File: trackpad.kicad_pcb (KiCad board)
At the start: 2 copper layers, 172 x 125.9 mm, 68 parts, among them J1 type-c-31-m-12, J10 Conn_01x01_Pin, J3 JST 3P, J5 Conn_01x07_Pin, J9 Conn_01x02_Pin, SW1 SW_Push, SW2 SW_Push, SW3 SW_Push, SW4 SW_Push, U1 RP2040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

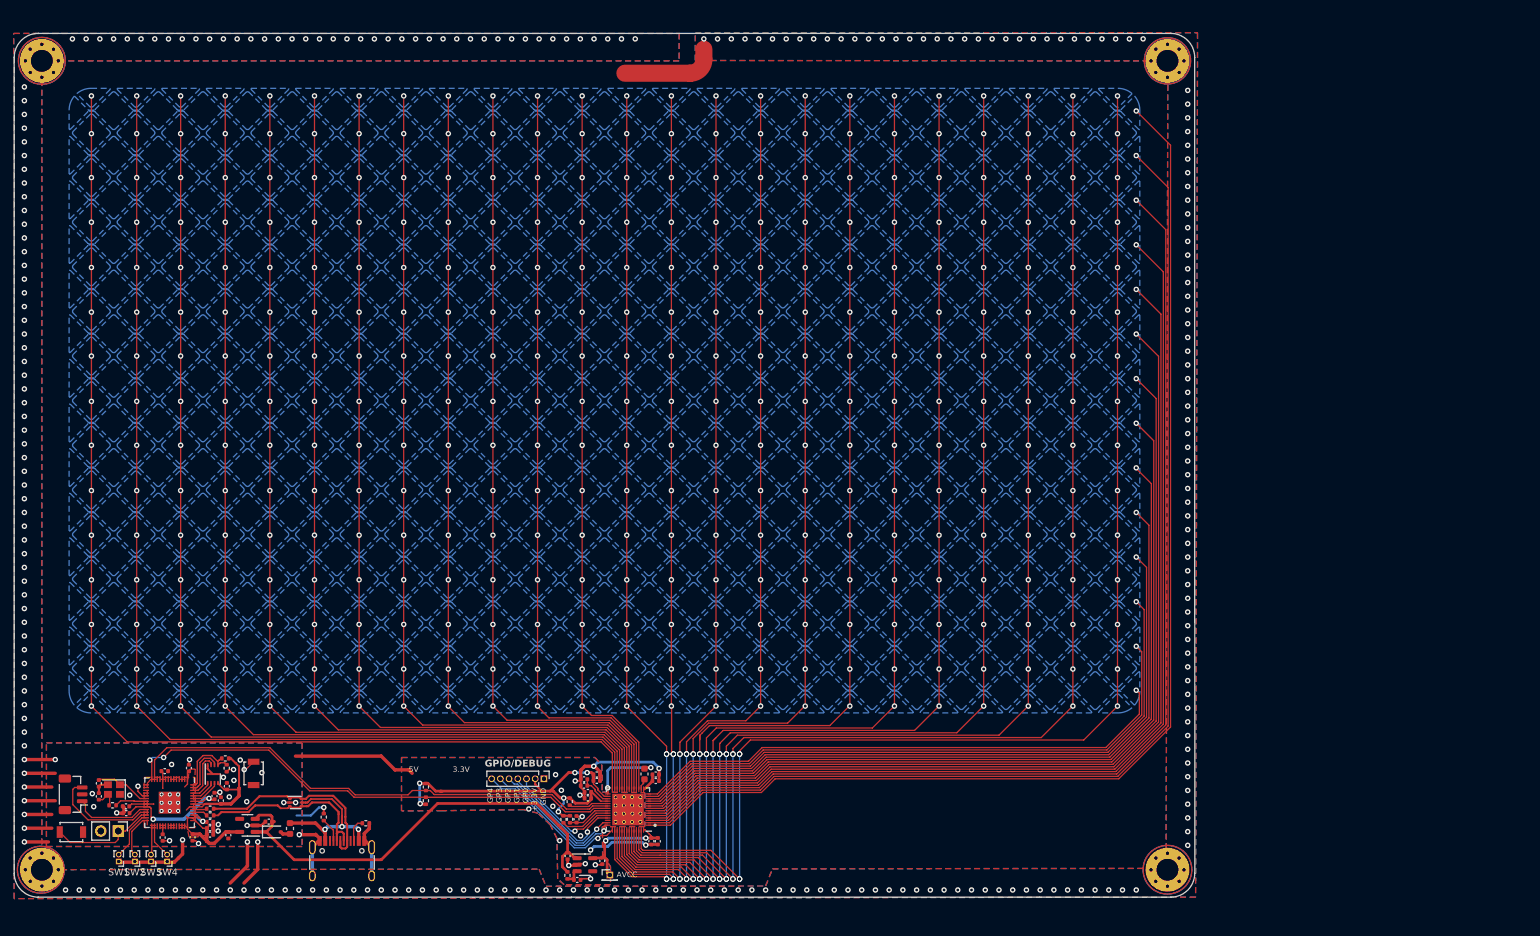
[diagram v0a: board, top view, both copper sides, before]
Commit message: made some adjustments to the gnd planes and connections
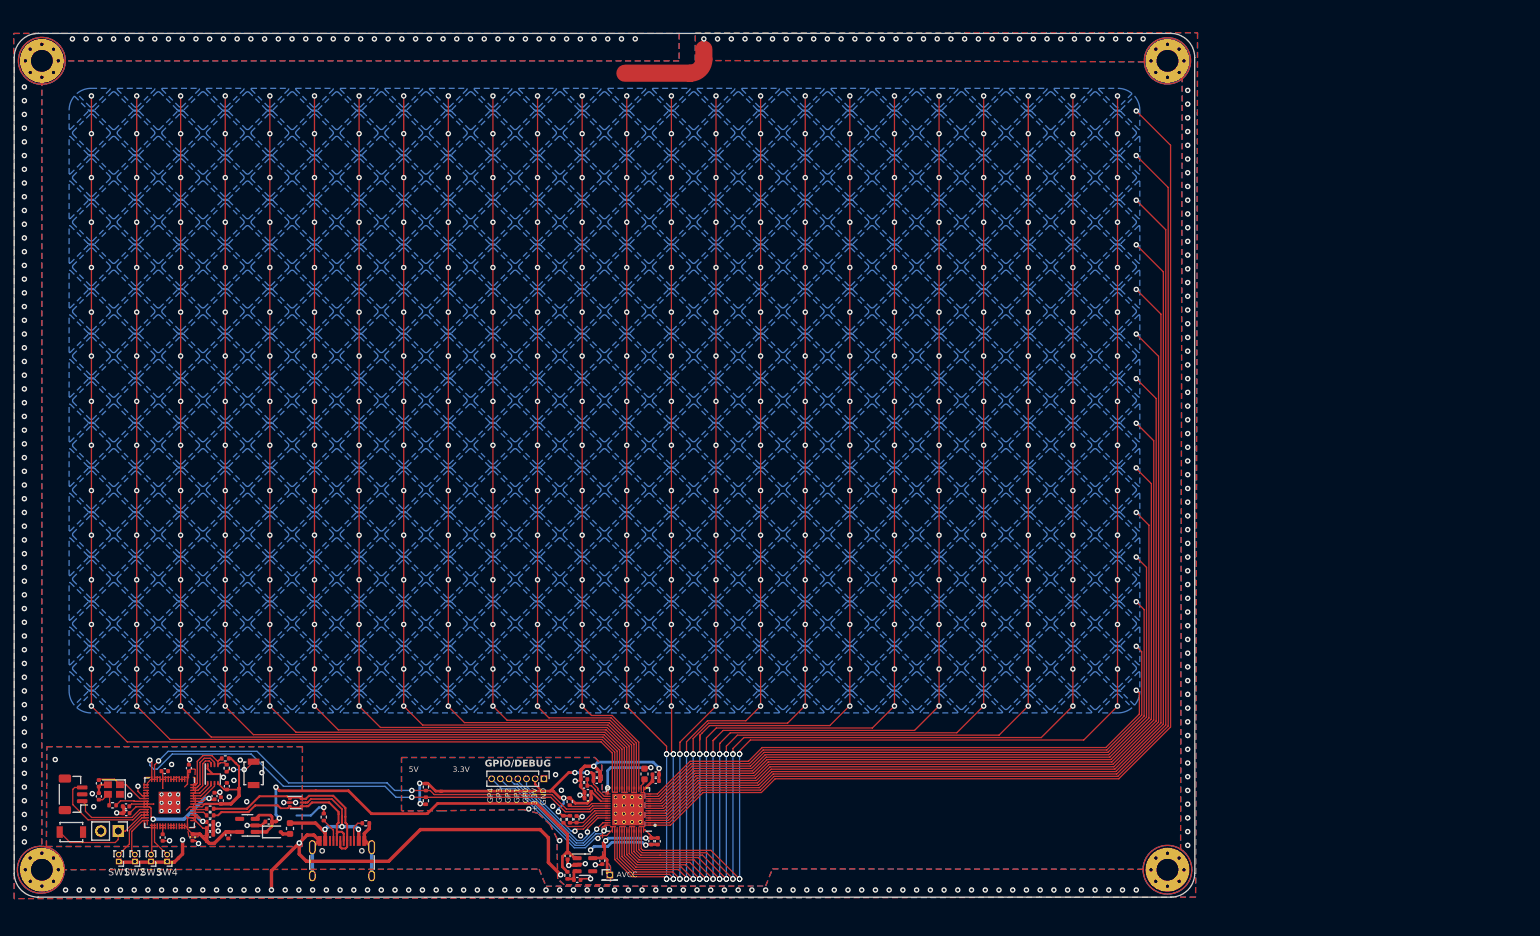
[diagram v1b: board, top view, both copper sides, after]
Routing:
- net (no net): track 31.9 -> 0.00 mm, vias 4 -> 2
- net GND: track 141.5 -> 168.2 mm, vias 317 -> 318
- net Net-(R2-Pad1): track 2.98 -> 4.53 mm
- net 5V: track 66.1 -> 67.6 mm, vias 0 -> 2
- net SDA: track 73.9 -> 72.5 mm, vias 0 -> 2
- net SCL: track 74.0 -> 75.1 mm

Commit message: rotated things in the PCB editor so its orientation matches intended use.
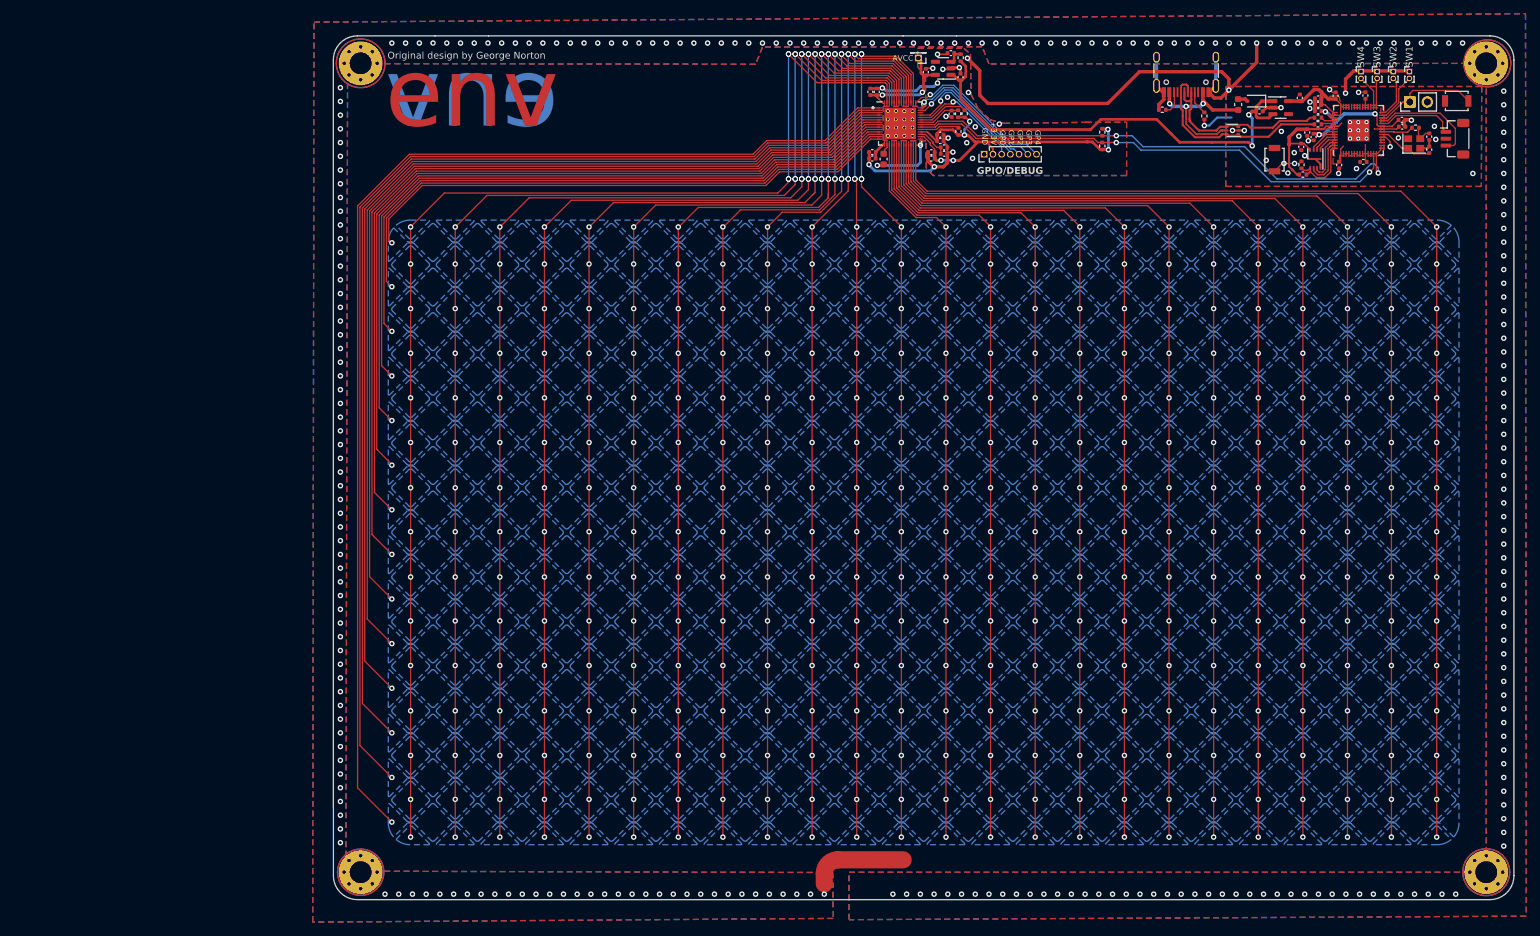
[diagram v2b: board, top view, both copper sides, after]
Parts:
- moved H3 241.4 mm to (239.0, 153.4), turned to 180 degrees
- moved H4 241.0 mm to (239.0, 35.6), turned to 180 degrees
- moved SW_RST1 228.2 mm to (234.7, 41.0), turned to 180 degrees
- moved J3 222.9 mm to (234.4, 46.5), turned to -90 degrees
- moved SW1 220.5 mm to (227.8, 36.8), turned to 0 degrees
- moved SW2 216.5 mm to (225.4, 36.8), turned to 0 degrees
- moved C13 216.4 mm to (230.7, 46.2), turned to -90 degrees
- moved J9 216.1 mm to (227.9, 41.2), turned to 90 degrees
- moved C12 214.7 mm to (230.7, 48.1), turned to 90 degrees
- moved R3 214.0 mm to (228.7, 44.9), turned to 0 degrees
- moved SW3 212.5 mm to (223.1, 36.8), turned to 0 degrees
- moved Y1 211.5 mm to (228.5, 47.2), turned to 0 degrees
- moved C3 211.5 mm to (226.7, 43.8), turned to 0 degrees
- moved C8 210.7 mm to (226.7, 44.8), turned to 0 degrees
- moved SW4 208.6 mm to (220.7, 36.8), turned to 0 degrees
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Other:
- board size 172 x 125.9 mm -> 172 x 125.8 mm
- board text added: "Original design by George Norton"
- board text added: "env"
- board text removed: "3.3V"
- board text removed: "5V"

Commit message: added some art, might remove
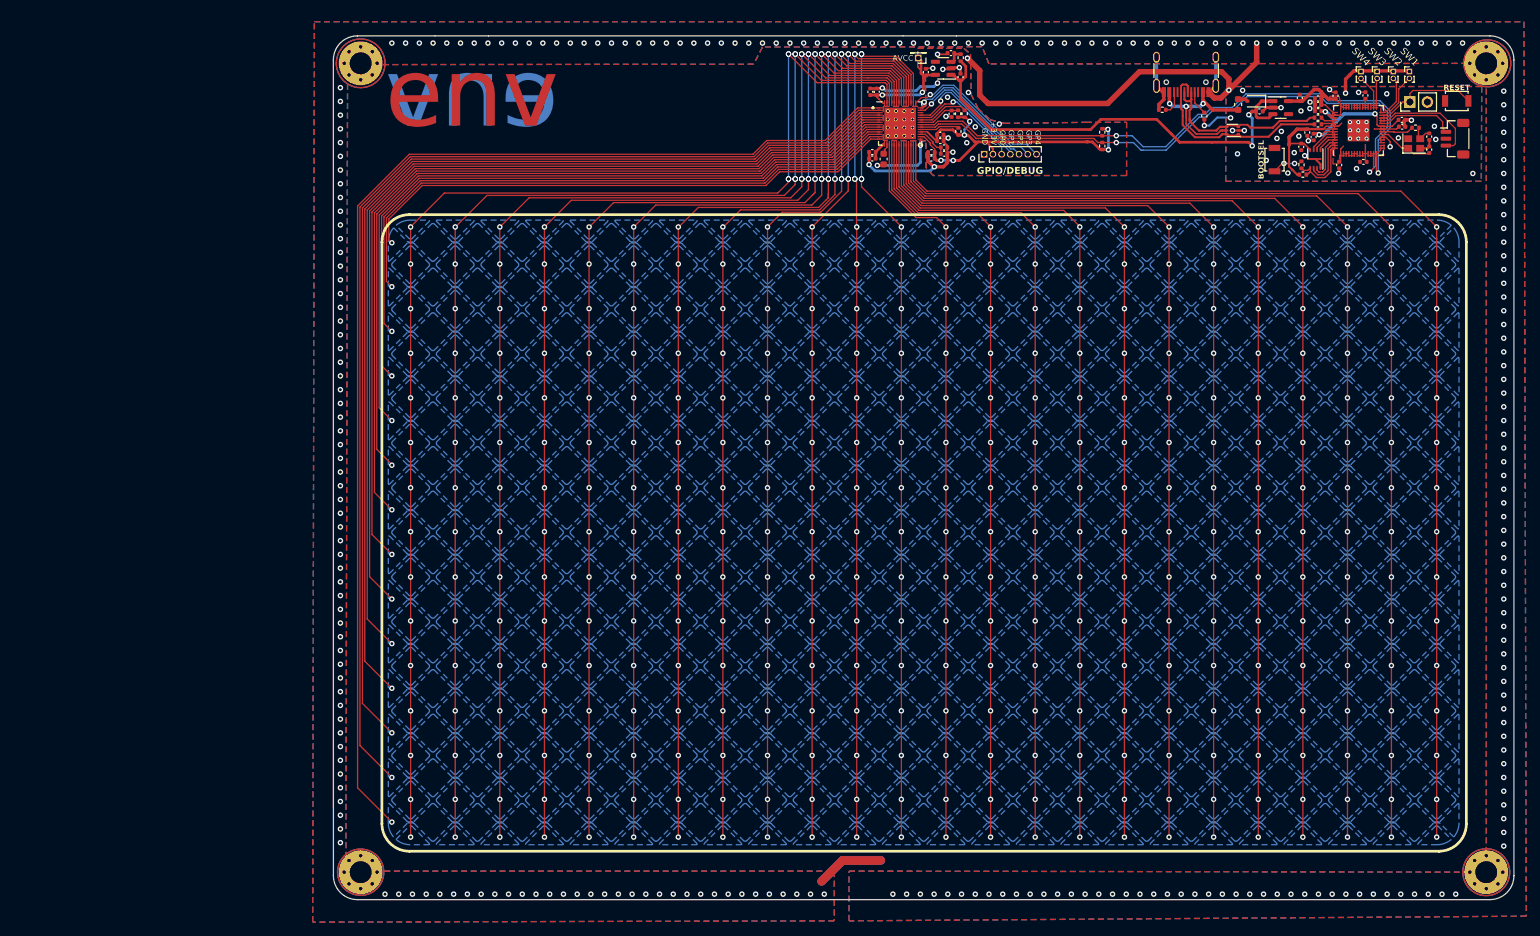
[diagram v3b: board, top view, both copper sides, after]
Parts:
- added G***: LOGO, extras:altai, B.Cu at (157.1, 94.2)
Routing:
- net SDA: track 72.5 -> 87.0 mm
- net SCL: track 75.1 -> 86.9 mm
- net GND: track 168.2 -> 174.0 mm, vias 318 -> 324
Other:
- board text added: "BOOTSEL"
- board text added: "Original design by George Norton | Peacock"
- board text added: "RESET"
- board text removed: "Original design by George Norton"
